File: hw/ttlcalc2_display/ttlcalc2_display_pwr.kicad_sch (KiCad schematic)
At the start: 31 parts, among them J2 HV_PWR, J3 5V_PWR, U13 74LS04, U14 74LS04, U15 74LS04, U17 74LS08, U5 74LS04, U6 74LS04, U7 74LS04, U8 74LS04

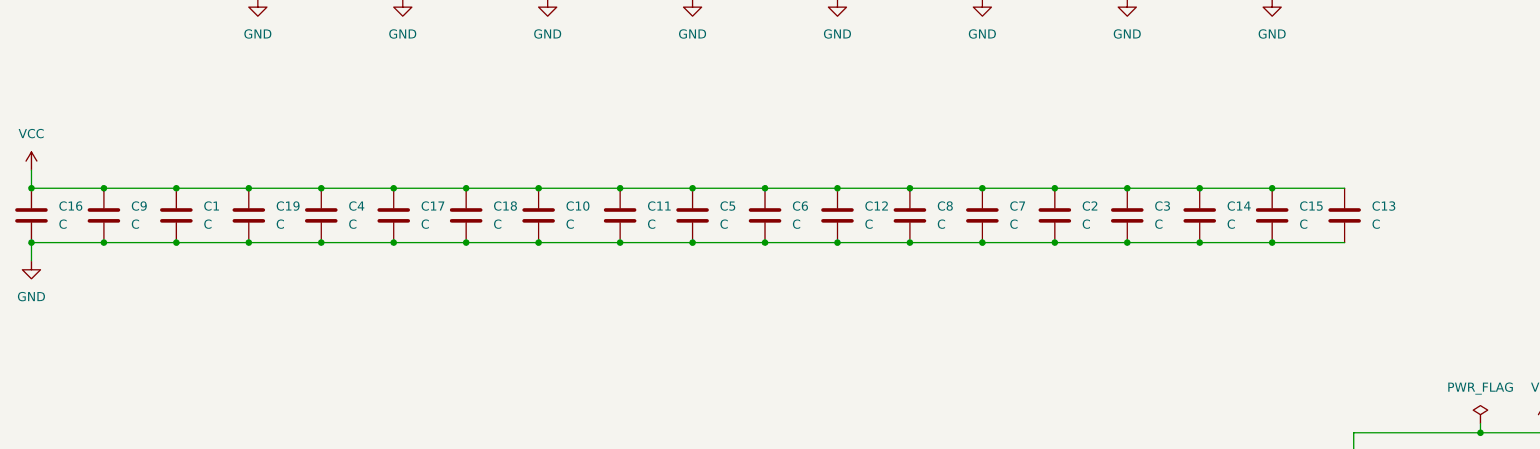
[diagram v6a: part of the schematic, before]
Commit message: Minor display hardware revisions
Add anti-ghosting inter-cathode resistors to nixies
Adjust component values based on experiments
Change from individual netclass labels to rule areas
Tweak traces on display board
Update .gitignore to ignore KiCad lock files
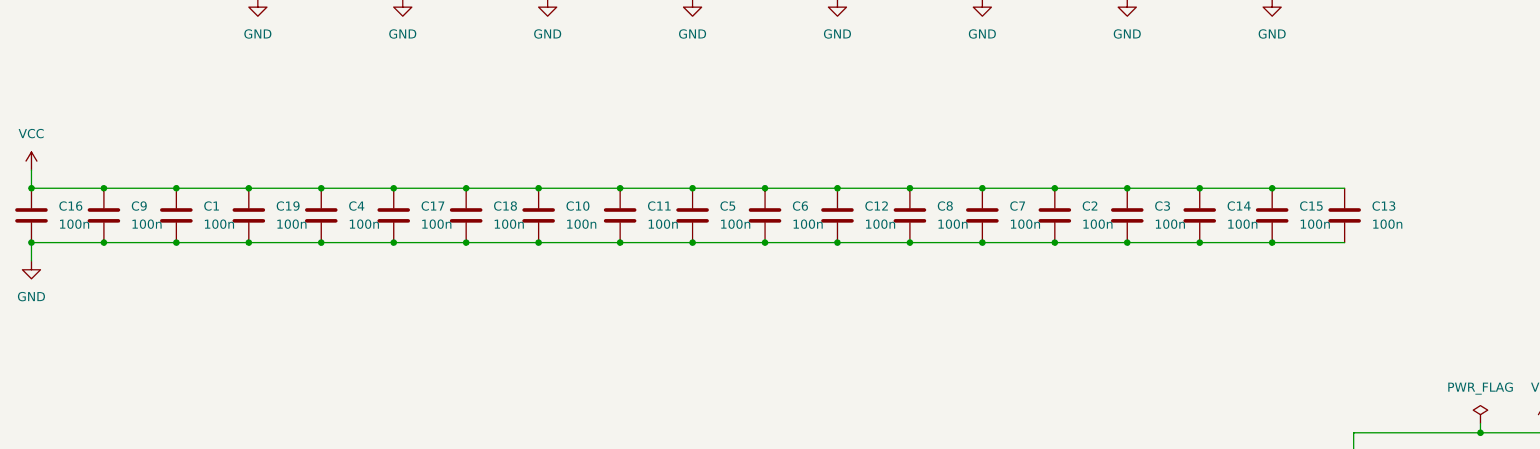
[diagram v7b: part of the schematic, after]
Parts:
- C1, C10, C11, C12, C13, C14, C15, C16, C17, C18, C19, C2, C3, C4, C5, C6, C7, C8, C9: value C -> 100n
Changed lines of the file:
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@@
 			)
 		)
-		(property "Value" "C"
+		(property "Value" "100n"
 			(at 172.72 81.2799 0)
 			(effects
@@
 			)
 		)
-		(property "Value" "C"
+		(property "Value" "100n"
 			(at 90.17 81.2799 0)
 			(effects
@@
 			)
 		)
-		(property "Value" "C"
+		(property "Value" "100n"
 			(at 100.33 81.2799 0)
 			(effects
@@
 			)
 		)
-		(property "Value" "C"
+		(property "Value" "100n"
 			(at 80.01 81.2799 0)
 			(effects
@@
 			)
 		)
-		(property "Value" "C"
+		(property "Value" "100n"
 			(at 39.37 81.2799 0)
 			(effects
@@
 			)
 		)
-		(property "Value" "C"
+		(property "Value" "100n"
 			(at 69.85 81.2799 0)
 			(effects
@@
 			)
 		)
-		(property "Value" "C"
+		(property "Value" "100n"
 			(at 132.08 81.2799 0)
 			(effects
@@
 			)
 		)
-		(property "Value" "C"
+		(property "Value" "100n"
 			(at 182.88 81.2799 0)
 			(effects
@@
 			)
 		)
-		(property "Value" "C"
+		(property "Value" "100n"
 			(at 121.92 81.2799 0)
 			(effects
@@
 			)
 		)
-		(property "Value" "C"
+		(property "Value" "100n"
 			(at 213.36 81.2799 0)
 			(effects
@@
 			)
 		)
-		(property "Value" "C"
+		(property "Value" "100n"
 			(at 162.56 81.2799 0)
 			(effects
@@
 			)
 		)
-		(property "Value" "C"
+		(property "Value" "100n"
 			(at 193.04 81.2799 0)
 			(effects
@@
 			)
 		)
-		(property "Value" "C"
+		(property "Value" "100n"
 			(at 142.24 81.2799 0)
 			(effects
@@
 			)
 		)
-		(property "Value" "C"
+		(property "Value" "100n"
 			(at 29.21 81.2799 0)
 			(effects
@@
 			)
 		)
-		(property "Value" "C"
+		(property "Value" "100n"
 			(at 59.69 81.2799 0)
 			(effects
@@
 			)
 		)
-		(property "Value" "C"
+		(property "Value" "100n"
 			(at 152.4 81.2799 0)
 			(effects
@@
 			)
 		)
-		(property "Value" "C"
+		(property "Value" "100n"
 			(at 203.2 81.2799 0)
 			(effects
@@
 			)
 		)
-		(property "Value" "C"
+		(property "Value" "100n"
 			(at 49.53 81.2799 0)
 			(effects
@@
 			)
 		)
-		(property "Value" "C"
+		(property "Value" "100n"
 			(at 111.76 81.2799 0)
 			(effects
